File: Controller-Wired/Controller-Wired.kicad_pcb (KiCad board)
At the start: 2 copper layers, 7 parts, among them J1 Conn_02x20_Odd_Even, U1 STM32F103CBTx

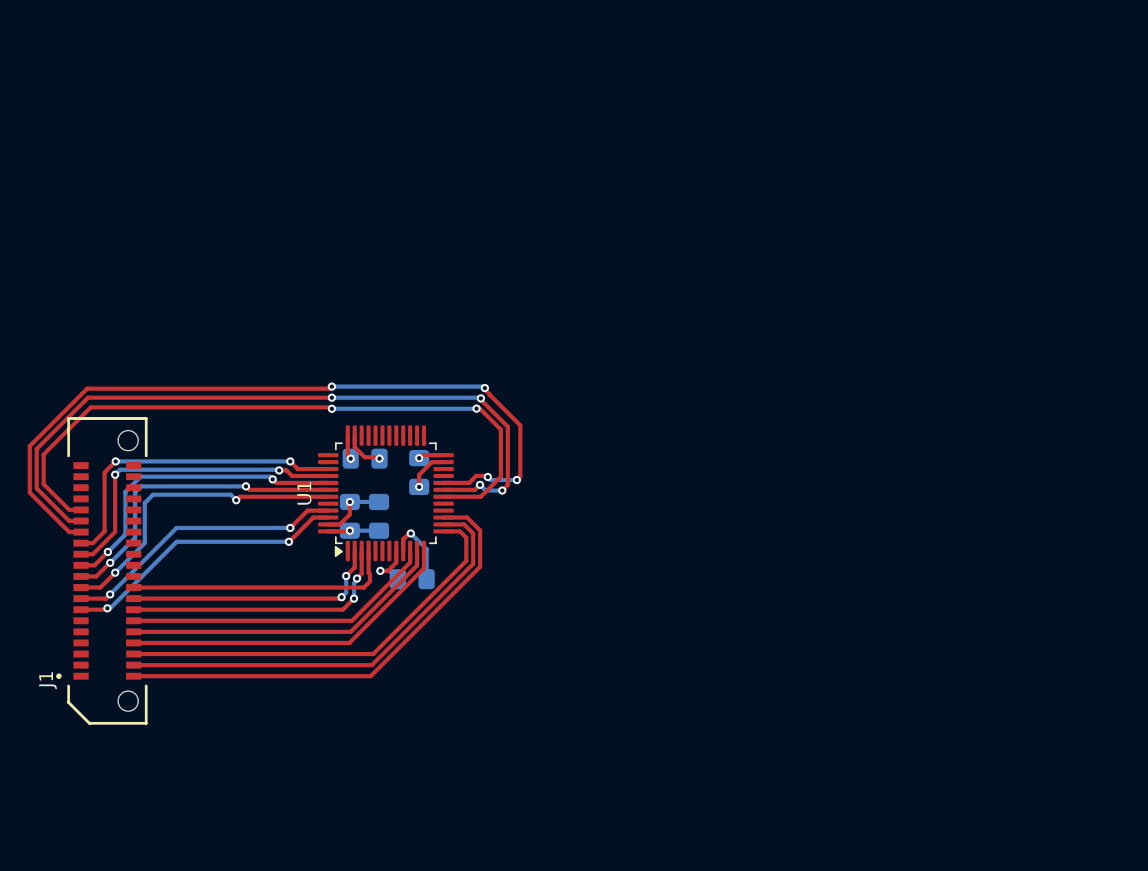
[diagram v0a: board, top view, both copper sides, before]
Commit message: Started Controller Routing
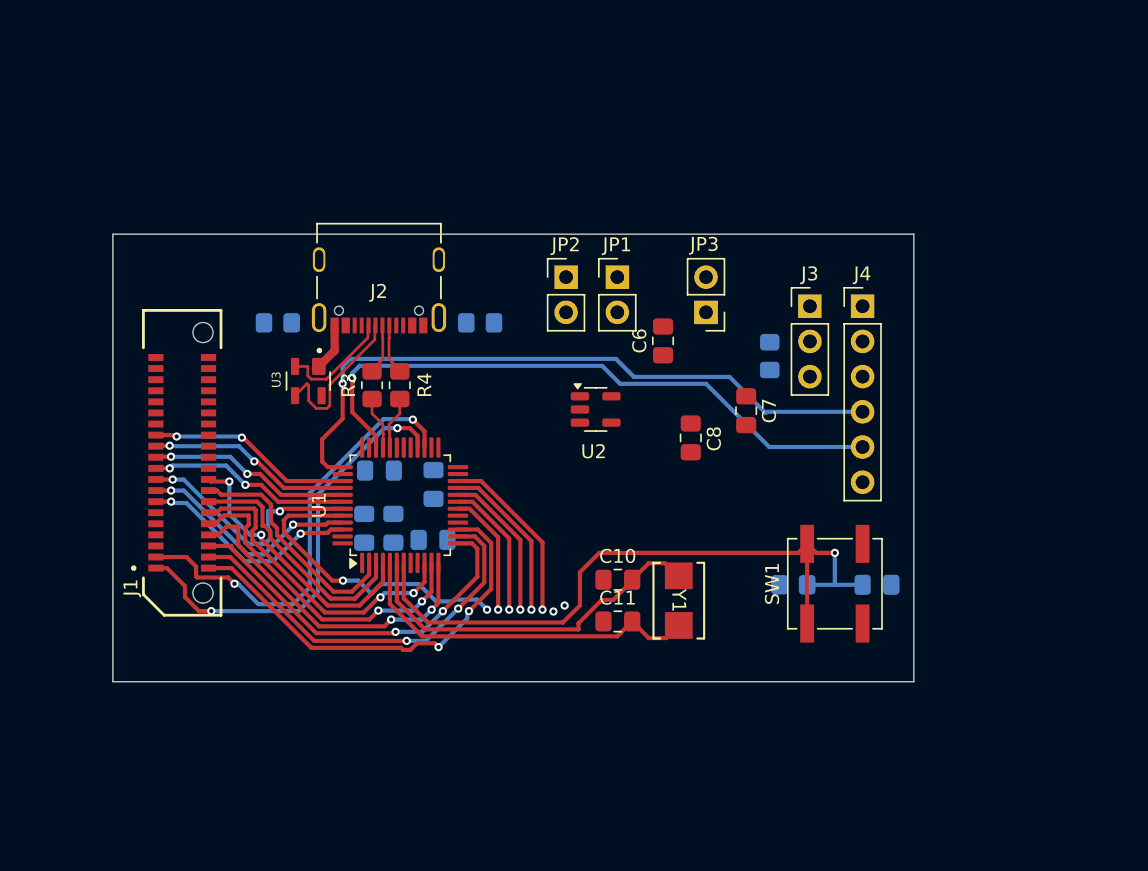
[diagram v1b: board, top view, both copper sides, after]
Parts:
- added C10: 10pF, Capacitor_SMD:C_0805_2012Metric_Pad1.18x1.45mm_HandSolder, F.Cu at (128.7, 77.2)
- added C11: 10pF, Capacitor_SMD:C_0805_2012Metric_Pad1.18x1.45mm_HandSolder, F.Cu at (128.7, 80.2)
- added C6: 1uF, Capacitor_SMD:C_0805_2012Metric_Pad1.18x1.45mm_HandSolder, F.Cu at (132.0, 60.0)
- added C7: 10uF, Capacitor_SMD:C_0805_2012Metric_Pad1.18x1.45mm_HandSolder, F.Cu at (138.0, 65.0)
- added C8: 0.1uF, Capacitor_SMD:C_0805_2012Metric_Pad1.18x1.45mm_HandSolder, F.Cu at (134.0, 67.0)
- added C9: 0.1uF, Capacitor_SMD:C_0805_2012Metric_Pad1.18x1.45mm_HandSolder, B.Cu at (147.4, 77.6)
- added J2: USB_C_Receptacle, Controller:AMPHENOL_12402012E212A, F.Cu at (111.5, 54.1)
- added J3: Conn_01x03, Connector_PinHeader_2.54mm:PinHeader_1x03_P2.54mm_Vertical, F.Cu at (142.6, 57.5)
- added J4: Conn_01x06, Connector_PinHeader_2.54mm:PinHeader_1x06_P2.54mm_Vertical, F.Cu at (146.4, 57.5)
- added JP1: Jumper_2_Open, Connector_PinHeader_2.54mm:PinHeader_1x02_P2.54mm_Vertical, F.Cu at (128.7, 55.4)
- added JP2: Jumper_2_Open, Connector_PinHeader_2.54mm:PinHeader_1x02_P2.54mm_Vertical, F.Cu at (125.0, 55.4)
- added JP3: Jumper_2_Open, Connector_PinHeader_2.54mm:PinHeader_1x02_P2.54mm_Vertical, F.Cu at (135.1, 57.9)
- added R1: 5k1, Resistor_SMD:R_0805_2012Metric_Pad1.20x1.40mm_HandSolder, B.Cu at (104.2, 58.7)
- added R2: 5k1, Resistor_SMD:R_0805_2012Metric_Pad1.20x1.40mm_HandSolder, B.Cu at (118.8, 58.7)
- added R3: 22, Resistor_SMD:R_0805_2012Metric_Pad1.20x1.40mm_HandSolder, F.Cu at (113.0, 63.2)
- added R4: 22, Resistor_SMD:R_0805_2012Metric_Pad1.20x1.40mm_HandSolder, F.Cu at (111.0, 63.2)
- added R5: 10k, Resistor_SMD:R_0805_2012Metric_Pad1.20x1.40mm_HandSolder, B.Cu at (139.7, 61.1)
- added R6: 10k, Resistor_SMD:R_0805_2012Metric_Pad1.20x1.40mm_HandSolder, B.Cu at (141.4, 77.6)
- added SW1: SW_Push, Button_Switch_SMD:SW_SPST_B3SL-1002P, F.Cu at (144.4, 77.5)
- added U2: AP131-33, Package_TO_SOT_SMD:SOT-23-5, F.Cu at (127.1, 65.0)
- added U3: TPD2E001DZDR, Controller:SOT192P237X122-4N, F.Cu at (106.4, 62.9)
- added Y1: Crystal, Controller:XTAL_ABM3-8.000MHZ-D2Y-T_ABR, F.Cu at (133.1, 78.7)
- moved J1 9.49 mm to (97.3, 68.8)
- moved C4 3.21 mm to (115.4, 74.4)
- moved C3 1.35 mm to (110.4, 73.5)
- moved C5 1.35 mm to (112.5, 73.5)
- moved C1 1.35 mm to (115.4, 70.4)
- moved C2 1.35 mm to (111.5, 69.4)
- moved U1 1.35 mm to (113.0, 71.9)
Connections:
- U1 pad 34: unconnected-(U1-PA13-Pad34) -> SWDIO
- U1 pad 37: unconnected-(U1-PA14-Pad37) -> SWCLK
- U1 pad 44: unconnected-(U1-BOOT0-Pad44) -> BOOT
- U1 pad 5: unconnected-(U1-PD0-Pad5) -> Net-(U1-PD0)
- U1 pad 6: unconnected-(U1-PD1-Pad6) -> Net-(U1-PD1)
- U1 pad 7: unconnected-(U1-NRST-Pad7) -> NRST
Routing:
- net NRST: track 0.00 -> 50.5 mm, vias 0 -> 1
- net SWCLK: track 0.00 -> 48.5 mm, vias 0 -> 1
- net SWDIO: track 0.00 -> 45.6 mm, vias 0 -> 1
- net COL2: track 56.3 -> 10.9 mm, vias 4 -> 1
- net COL1: track 52.6 -> 9.93 mm, vias 4 -> 1
- net COL0: track 48.7 -> 8.98 mm, vias 2 -> 1
- net COL14: track 0.00 -> 32.5 mm, vias 0 -> 2
- net COL15: track 0.00 -> 31.3 mm, vias 0 -> 2
- net Net-(U1-PD1): track 0.00 -> 26.6 mm
- net Net-(U1-PD0): track 0.00 -> 26.1 mm
- net BOOT: track 0.00 -> 22.9 mm, vias 0 -> 2
- net D-: track 0.00 -> 15.1 mm
- net COL11: track 0.00 -> 12.8 mm, vias 0 -> 1
- net VDD: track 12.6 -> 0.00 mm, vias 4 -> 0
- net D+: track 0.00 -> 11.9 mm
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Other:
- board outline added: 57.8 x 32.3 mm
- copper layers 2 -> 4

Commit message: Reworking the layout, and changed the ESD Protection
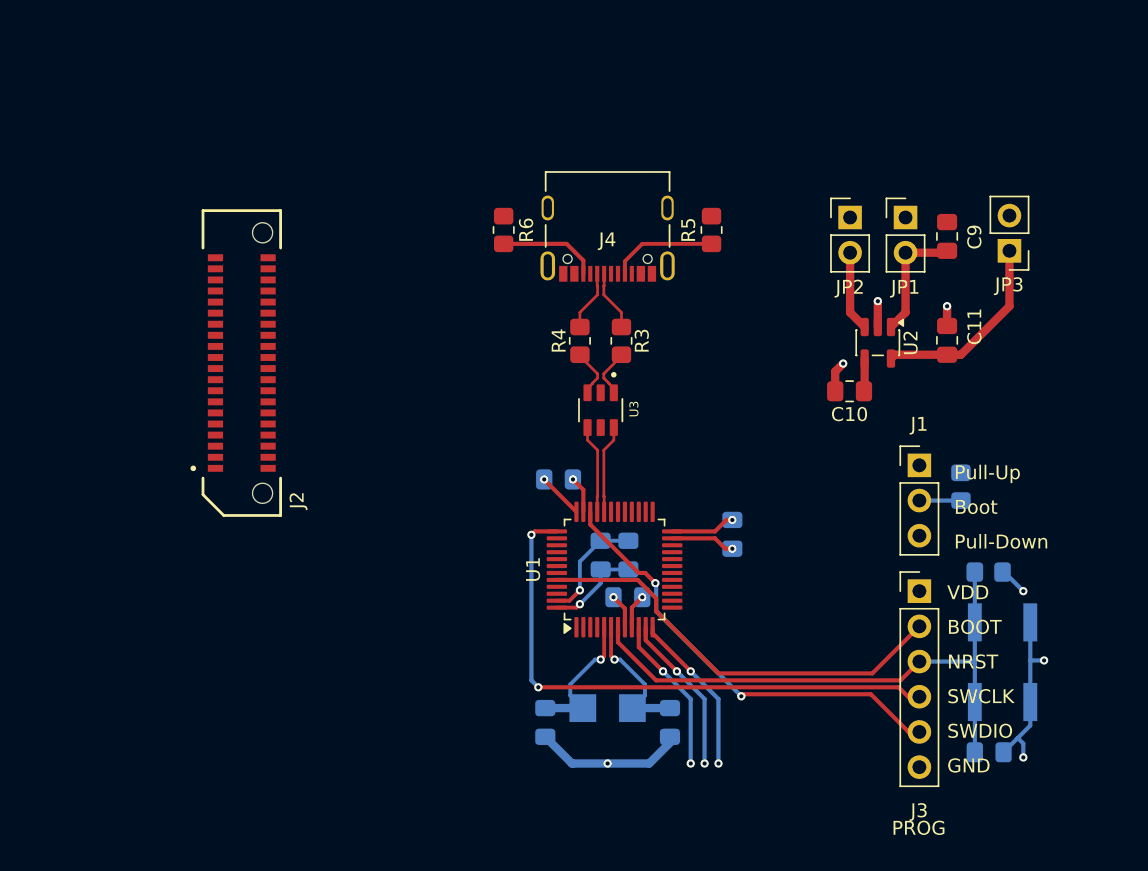
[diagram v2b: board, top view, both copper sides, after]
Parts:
- C1, C2: value 100nF -> 10pF
- C10: value 10pF -> 0.1uF
- C11: value 10pF -> 10uF
- C4: value 10nF -> 100nF
- C5: value 4.7uF -> 100nF
- C6: value 1uF -> 4.7uF; moved to B.Cu
- C7: value 10uF -> 10nF; moved to B.Cu
- C8, SW1, Y1: moved to B.Cu
- C9: value 0.1uF -> 1uF; moved to F.Cu
- J1: value Conn_02x20_Odd_Even -> Conn_01x03; footprint Controller:SAMTEC_ERM8-020-X-X-DV -> Connector_PinHeader_2.54mm:PinHeader_1x03_P2.54mm_Vertical
- J2: value USB_C_Receptacle -> Conn_02x20_Odd_Even; footprint Controller:AMPHENOL_12402012E212A -> Controller:SAMTEC_ERM8-020-X-X-DV
- J3: value Conn_01x03 -> Conn_01x06; footprint Connector_PinHeader_2.54mm:PinHeader_1x03_P2.54mm_Vertical -> Connector_PinHeader_2.54mm:PinHeader_1x06_P2.54mm_Vertical
- J4: value Conn_01x06 -> USB_C_Receptacle; footprint Connector_PinHeader_2.54mm:PinHeader_1x06_P2.54mm_Vertical -> Controller:AMPHENOL_12402012E212A
- R1, R2: value 5k1 -> 10k
- R5, R6: value 10k -> 5k1; moved to F.Cu
- U3: value TPD2E001DZDR -> USBLC6-2SC6; footprint Controller:SOT192P237X122-4N -> Controller:SOT95P280X145-6N
- moved R1 54.4 mm to (155.5, 76.7), turned to 0 degrees
- moved J1 53.2 mm to (150.5, 69.0), turned to 0 degrees
- moved R2 36.7 mm to (153.5, 70.5), turned to -90 degrees
- moved R6 33.0 mm to (120.5, 52.0), turned to -90 degrees
- moved C8 31.3 mm to (155.5, 89.7), turned to 0 degrees
- moved C11 31.2 mm to (152.5, 60.0), turned to 90 degrees
- moved C2 27.7 mm to (132.5, 87.5), turned to 90 degrees
- moved C3 26.6 mm to (137.0, 74.0), turned to 90 degrees
- moved C9 25.6 mm to (152.5, 52.5), turned to 90 degrees
- moved JP3 22.3 mm to (157.0, 53.5)
- moved J3 22.0 mm to (150.5, 78.1)
- moved C10 21.6 mm to (145.5, 63.6), turned to 180 degrees
- moved JP1 21.2 mm to (149.5, 51.1)
- moved U3 21.2 mm to (127.5, 65.0)
- moved JP2 20.9 mm to (145.5, 51.1)
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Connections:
- C1 pad 2: VDD -> Net-(U1-PD0)
- C10 pad 1: GND -> Net-(U2-BP)
- C10 pad 2: Net-(U1-PD1) -> GND
- C11 pad 1: GND -> Net-(JP3-A)
- C11 pad 2: Net-(U1-PD0) -> GND
- C2 pad 2: VDD -> Net-(U1-PD1)
- C6 pad 1: Net-(JP1-B) -> GND
- C6 pad 2: GND -> VDD
- C7 pad 1: Net-(JP3-A) -> GND
- C7 pad 2: GND -> VDD
- C8 pad 1: Net-(U2-BP) -> NRST
- C9 pad 1: NRST -> Net-(JP1-B)
- J3 pad 2: Net-(J3-Pin_2) -> BOOT
- J3 pad 3: GND -> NRST
- R1 pad 1: Net-(J2-CC2) -> NRST
- R1 pad 2: GND -> VDD
- R2 pad 1: Net-(J2-CC1) -> BOOT
- R2 pad 2: GND -> Net-(J1-Pin_2)
- R3 pad 1: D- -> D_1-
- R3 pad 2: USB- -> D-
- R4 pad 1: D+ -> D_1+
- R4 pad 2: USB+ -> D+
- R5 pad 1: BOOT -> Net-(J4-CC1)
- R5 pad 2: Net-(J3-Pin_2) -> GND
- R6 pad 1: NRST -> GND
- R6 pad 2: VDD -> Net-(J4-CC2)
- U3 pad 1: GND -> D-
- U3 pad 2: D+ -> GND
- U3 pad 3: D- -> D+
- U3 pad 4: VBUS -> USB+
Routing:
- net GND: track 3.43 -> 47.1 mm, vias 0 -> 10
- net COL14: track 32.5 -> 0.00 mm, vias 2 -> 0
- net ROW5: track 31.5 -> 0.00 mm, vias 2 -> 0
- net COL15: track 31.3 -> 0.00 mm, vias 2 -> 0
- net ROW4: track 29.0 -> 0.00 mm, vias 2 -> 0
- net ROW3: track 27.4 -> 0.00 mm, vias 2 -> 0
- net ENC_SW: track 20.0 -> 0.00 mm, vias 2 -> 0
- net VDD: track 0.00 -> 19.4 mm, vias 0 -> 5
- net COL7: track 17.8 -> 0.00 mm, vias 2 -> 0
- net ENC_B: track 17.8 -> 0.00 mm
- net ENC_A: track 17.0 -> 0.00 mm
- net Net-(U1-PD1): track 26.6 -> 10.2 mm, vias 0 -> 1
- net COL8: track 16.4 -> 0.00 mm, vias 2 -> 0
- net COL9: track 16.2 -> 0.00 mm, vias 2 -> 0
- net Net-(U1-PD0): track 26.1 -> 10.2 mm, vias 0 -> 1
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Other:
- board outline removed
- board text added: "BOOT"
- board text added: "Boot"
- board text added: "GND"
- board text added: "NRST"
- board text added: "PROG"
- board text added: "Pull-Down"
- board text added: "Pull-Up"
- board text added: "SWCLK"
- board text added: "SWDIO"
- board text added: "VDD"

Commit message: Finished First Rev Of Both PCB's, after testing fits in freecad, will  move onto ordrering board
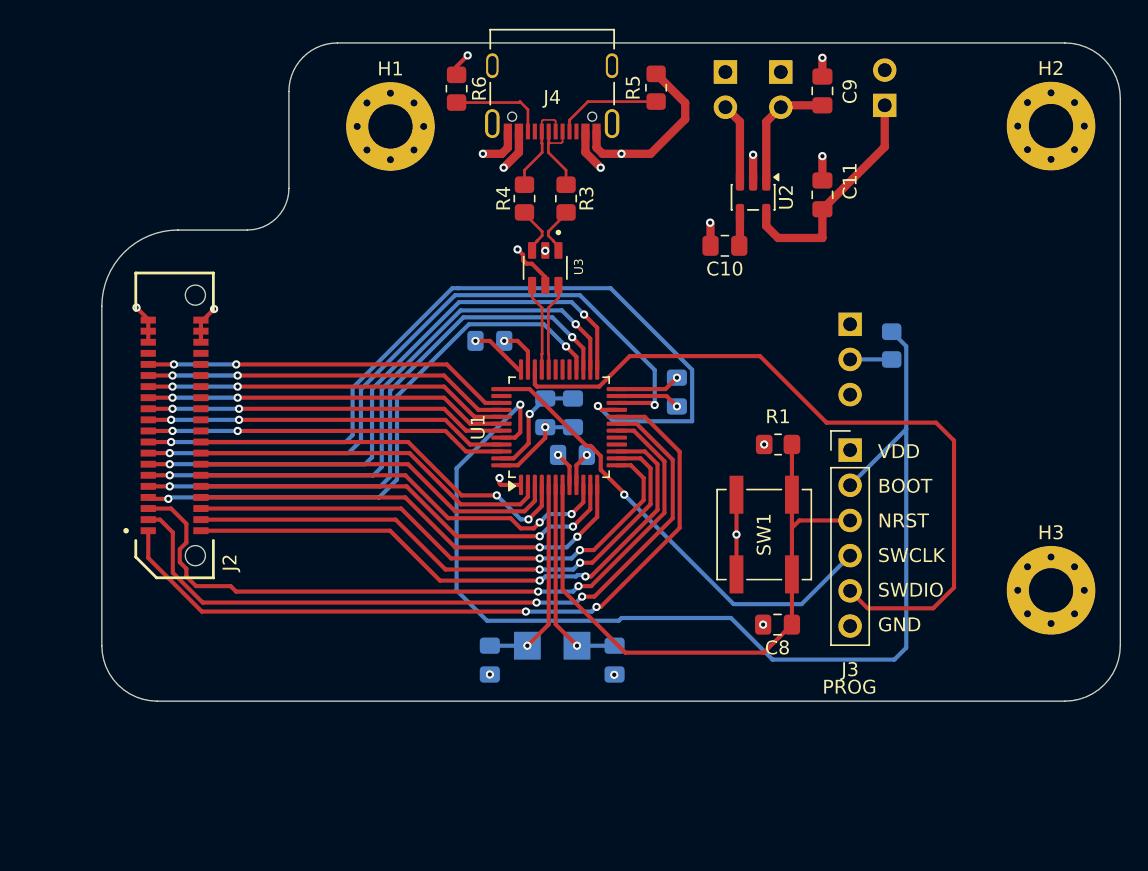
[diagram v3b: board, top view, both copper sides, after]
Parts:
- added H1: MountingHole, MountingHole:MountingHole_3.2mm_M3_Pad_Via, F.Cu at (112.3, 44.5)
- added H2: MountingHole, MountingHole:MountingHole_3.2mm_M3_Pad_Via, F.Cu at (160.0, 44.5)
- added H3: MountingHole, MountingHole:MountingHole_3.2mm_M3_Pad_Via, F.Cu at (160.0, 78.0)
- C8, R1, SW1: moved to F.Cu
- J1, JP1, JP2, JP3: moved to B.Cu
- moved SW1 19.5 mm to (139.3, 74.0)
- moved C8 17.8 mm to (140.3, 80.5), turned to 180 degrees
- moved R1 17.8 mm to (140.3, 67.5), turned to 180 degrees
- moved C10 13.8 mm to (136.5, 53.1)
- moved C11 13.8 mm to (143.5, 49.5)
- moved C9 13.8 mm to (143.5, 42.0)
- moved JP1 13.8 mm to (140.5, 40.6), turned to 180 degrees
- moved JP2 13.8 mm to (136.5, 40.6), turned to 180 degrees
- moved JP3 13.8 mm to (148.0, 43.0), turned to 0 degrees
- moved U2 13.8 mm to (138.5, 49.6)
- moved J1 11.3 mm to (145.5, 58.8), turned to 180 degrees
- moved J3 11.3 mm to (145.5, 67.9)
- moved R2 11.3 mm to (148.5, 60.3)
- moved C4 11.2 mm to (119.5, 60.0)
- moved C5 11.0 mm to (123.5, 65.2)
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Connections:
- U1 pad 18: COL0 -> COL13
- U1 pad 19: COL1 -> COL14
- U1 pad 20: COL2 -> COL15
- U1 pad 21: COL10 -> COL7
- U1 pad 22: COL11 -> COL8
- U1 pad 25: COL12 -> COL9
- U1 pad 26: COL13 -> COL10
- U1 pad 27: COL14 -> COL11
- U1 pad 28: COL15 -> COL12
- U1 pad 39: COL3 -> COL0
- U1 pad 40: COL4 -> COL1
- U1 pad 41: COL5 -> COL2
- U1 pad 42: COL6 -> COL3
- U1 pad 43: COL7 -> COL4
- U1 pad 45: COL8 -> COL5
- U1 pad 46: COL9 -> COL6
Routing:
- net COL7: track 0.00 -> 60.7 mm, vias 0 -> 2
- net COL15: track 0.00 -> 55.5 mm, vias 0 -> 2
- net COL14: track 0.00 -> 53.9 mm, vias 0 -> 2
- net COL13: track 0.00 -> 52.8 mm, vias 0 -> 2
- net BOOT: track 30.9 -> 82.8 mm, vias 0 -> 1
- net COL8: track 0.00 -> 51.0 mm, vias 0 -> 2
- net COL9: track 0.00 -> 43.9 mm, vias 0 -> 2
- net ROW5: track 0.00 -> 43.3 mm, vias 0 -> 2
- net COL10: track 0.00 -> 43.2 mm, vias 0 -> 2
- net COL11: track 0.00 -> 42.5 mm, vias 0 -> 2
- net COL12: track 0.00 -> 41.6 mm, vias 0 -> 2
- net ROW4: track 0.00 -> 41.2 mm, vias 0 -> 2
- net ROW3: track 0.00 -> 39.1 mm, vias 0 -> 2
- net ENC_SW: track 0.00 -> 28.8 mm, vias 0 -> 2
- net ENC_B: track 0.00 -> 27.0 mm
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- added copper zone on In2.Cu, net GND
- added copper zone on In1.Cu, net VBUS
- added copper zone on In1.Cu, net VDD
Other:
- board outline added: 73.5 x 47.5 mm

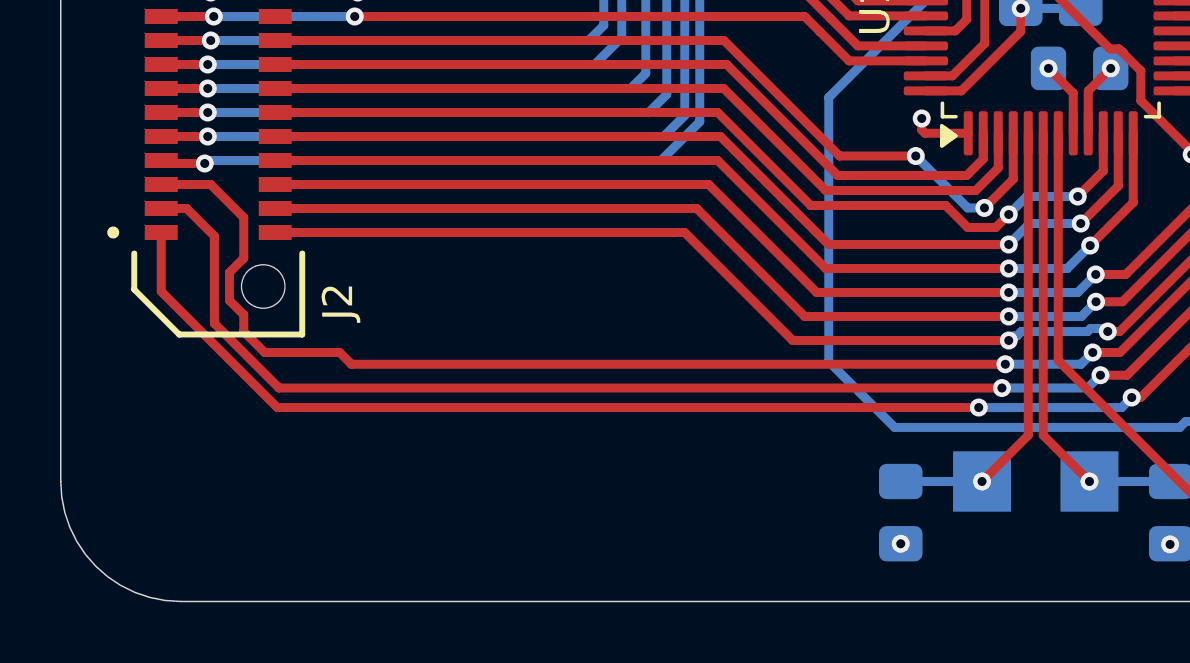
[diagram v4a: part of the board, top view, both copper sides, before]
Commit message: Added an extra mounting hole to controller board       -I Noticed some import errors on the usb-c fp when I cloned this on my laptop, go back and review all pads before sending to JLC
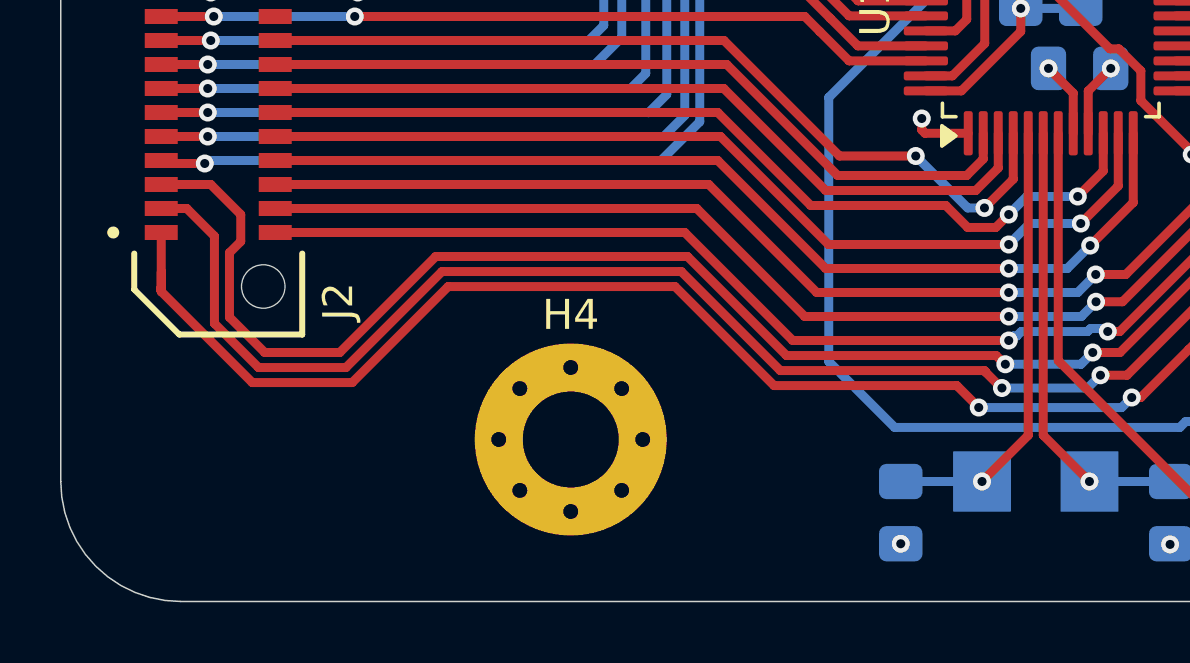
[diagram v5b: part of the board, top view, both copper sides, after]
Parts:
- added H4: MountingHole, MountingHole:MountingHole_3.2mm_M3_Pad_Via, F.Cu at (108.5, 80.6)
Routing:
- net COL15: track 55.5 -> 59.2 mm
- net COL14: track 53.9 -> 56.5 mm
- net COL13: track 52.8 -> 55.3 mm
